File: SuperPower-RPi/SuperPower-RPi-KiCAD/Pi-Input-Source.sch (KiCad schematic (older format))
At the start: 0 parts

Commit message: Added Input Protection Circuit for MWB.
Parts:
- added J?: Screw_Terminal_01x02, symbol Connector:Screw_Terminal_01x02
- added P1: USB_C_Plug, symbol Connector:USB_C_Plug
- added Q3: Q_PMOS_GSD, symbol Device:Q_PMOS_GSD
- added R3: 1k?, symbol Device:R
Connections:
- net labels added: GND
- wire segments 0 -> 14
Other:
- note added: "Primary USB Power Input"
- note added: "Solar or Other Input Power"
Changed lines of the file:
@@
 Comment4 ""
 $EndDescr
-Text HLabel 7600 2900 0    50   Output ~ 0
+Text HLabel 7300 2900 2    50   Output ~ 0
 Vout
-Text Notes 2350 4000 0    50   ~ 0
+Text Notes 6950 5750 0    50   ~ 0
 NOTE:\nProbably USB-C and screw-terminals for solar.  MicroUSB possible.
+$Comp
+L Device:Q_PMOS_GSD Q3
+U 1 1 5F703042
+P 6950 3000
+F 0 "Q3" V 7292 3000 50  0000 C CNN
+F 1 "Q_PMOS_GSD" V 7201 3000 50  0000 C CNN
+F 2 "" H 7150 3100 50  0001 C CNN
+F 3 "~" H 6950 3000 50  0001 C CNN
+	1    6950 3000
+	0    -1   -1   0
+$EndComp
+$Comp
+L power:GND #PWR05
+U 1 1 5F703EB6
+P 6950 3850
+F 0 "#PWR05" H 6950 3600 50  0001 C CNN
+F 1 "GND" H 6955 3677 50  0000 C CNN
+F 2 "" H 6950 3850 50  0001 C CNN
+F 3 "" H 6950 3850 50  0001 C CNN
+	1    6950 3850
+	1    0    0    -1
+$EndComp
+$Comp
+L Connector:USB_C_Plug P1
+U 1 1 5F704D8C
+P 4550 3900
+F 0 "P1" H 4657 5167 50  0000 C CNN
+F 1 "USB_C_Plug" H 4657 5076 50  0000 C CNN
+F 2 "" H 4700 3900 50  0001 C CNN
+F 3 "https://www.usb.org/sites/default/files/documents/usb_type-c.zip" H 4700 3900 50  0001 C CNN
+	1    4550 3900
+	1    0    0    -1
+$EndComp
+$Comp
+L power:GND #PWR04
+U 1 1 5F709AD2
+P 4400 5750
+F 0 "#PWR04" H 4400 5500 50  0001 C CNN
+F 1 "GND" H 4405 5577 50  0000 C CNN
+F 2 "" H 4400 5750 50  0001 C CNN
+F 3 "" H 4400 5750 50  0001 C CNN
+	1    4400 5750
+	1    0    0    -1
+$EndComp
+Wire Wire Line
+	4250 5500 4250 5650
+Wire Wire Line
+	4250 5650 4400 5650
+Wire Wire Line
+	4550 5650 4550 5500
+Wire Wire Line
+	4400 5750 4400 5650
+Connection ~ 4400 5650
+Wire Wire Line
+	4400 5650 4550 5650
+$Comp
+L Device:R R3
+U 1 1 5F70A531
+P 6950 3500
+F 0 "R3" H 7020 3546 50  0000 L CNN
+F 1 "1k?" H 7020 3455 50  0000 L CNN
+F 2 "" V 6880 3500 50  0001 C CNN
+F 3 "~" H 6950 3500 50  0001 C CNN
+	1    6950 3500
+	1    0    0    -1
+$EndComp
+Wire Wire Line
+	6950 3350 6950 3200
+Wire Wire Line
+	6950 3650 6950 3850
+Wire Wire Line
+	7150 2900 7300 2900
+Wire Wire Line
+	5150 2900 5550 2900
+Text Notes 4150 6150 0    50   ~ 0
+Primary USB Power Input
+$Comp
+L Connector:Screw_Terminal_01x02 J?
+U 1 1 5F70C370
+P 4500 1750
+F 0 "J?" H 4418 1425 50  0000 C CNN
+F 1 "Screw_Terminal_01x02" H 4418 1516 50  0000 C CNN
+F 2 "" H 4500 1750 50  0001 C CNN
+F 3 "~" H 4500 1750 50  0001 C CNN
+	1    4500 1750
+	-1   0    0    1
+$EndComp
+Wire Wire Line
+	4700 1650 5550 1650
+Wire Wire Line
+	5550 1650 5550 2900
+Connection ~ 5550 2900
+Wire Wire Line
+	5550 2900 6750 2900
+$Comp
+L power:GND #PWR?
+U 1 1 5F70CF53
+P 4750 1800
+F 0 "#PWR?" H 4750 1550 50  0001 C CNN
+F 1 "GND" H 4755 1627 50  0000 C CNN
+F 2 "" H 4750 1800 50  0001 C CNN
+F 3 "" H 4750 1800 50  0001 C CNN
+	1    4750 1800
+	1    0    0    -1
+$EndComp
+Wire Wire Line
+	4700 1750 4750 1750
+Wire Wire Line
+	4750 1750 4750 1800
+Text Notes 4100 2100 0    50   ~ 0
+Solar or Other Input Power
 $EndSCHEMATC

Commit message: Added charger circuitry, and updated boost converter.
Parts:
- gave numbers to parts that had none: 1
- renumbered R3 to R12
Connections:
- net labels added: D+, D-
- wire segments 14 -> 18
- no-connect marks 0 -> 12
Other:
- note added: "Should the USB VBUS be moved to after the input protection?"
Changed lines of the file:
@@
 $EndComp
 $Comp
-L power:GND #PWR05
+L power:GND #PWR0101
 U 1 1 5F703EB6
 P 6950 3850
-F 0 "#PWR05" H 6950 3600 50  0001 C CNN
+F 0 "#PWR0101" H 6950 3600 50  0001 C CNN
 F 1 "GND" H 6955 3677 50  0000 C CNN
 F 2 "" H 6950 3850 50  0001 C CNN
@@
 $EndComp
 $Comp
-L power:GND #PWR04
+L power:GND #PWR0102
 U 1 1 5F709AD2
 P 4400 5750
-F 0 "#PWR04" H 4400 5500 50  0001 C CNN
+F 0 "#PWR0102" H 4400 5500 50  0001 C CNN
 F 1 "GND" H 4405 5577 50  0000 C CNN
 F 2 "" H 4400 5750 50  0001 C CNN
@@
 	4400 5650 4550 5650
 $Comp
-L Device:R R3
+L Device:R R12
 U 1 1 5F70A531
 P 6950 3500
-F 0 "R3" H 7020 3546 50  0000 L CNN
+F 0 "R12" H 7020 3546 50  0000 L CNN
 F 1 "1k?" H 7020 3455 50  0000 L CNN
 F 2 "" V 6880 3500 50  0001 C CNN
@@
 Primary USB Power Input
 $Comp
-L Connector:Screw_Terminal_01x02 J?
+L Connector:Screw_Terminal_01x02 J3
 U 1 1 5F70C370
 P 4500 1750
-F 0 "J?" H 4418 1425 50  0000 C CNN
+F 0 "J3" H 4418 1425 50  0000 C CNN
 F 1 "Screw_Terminal_01x02" H 4418 1516 50  0000 C CNN
 F 2 "" H 4500 1750 50  0001 C CNN
@@
 Connection ~ 5550 2900
 Wire Wire Line
-	5550 2900 6750 2900
+	5550 2900 5800 2900
 $Comp
-L power:GND #PWR?
+L power:GND #PWR010
 U 1 1 5F70CF53
 P 4750 1800
-F 0 "#PWR?" H 4750 1550 50  0001 C CNN
+F 0 "#PWR010" H 4750 1550 50  0001 C CNN
 F 1 "GND" H 4755 1627 50  0000 C CNN
 F 2 "" H 4750 1800 50  0001 C CNN
@@
 Text Notes 4100 2100 0    50   ~ 0
 Solar or Other Input Power
+$Comp
+L power:PWR_FLAG #FLG0101
+U 1 1 5F7A3576
+P 4800 1750
+F 0 "#FLG0101" H 4800 1825 50  0001 C CNN
+F 1 "PWR_FLAG" V 4800 1878 50  0001 L CNN
+F 2 "" H 4800 1750 50  0001 C CNN
+F 3 "~" H 4800 1750 50  0001 C CNN
+	1    4800 1750
+	0    1    1    0
+$EndComp
+Wire Wire Line
+	4800 1750 4750 1750
+Connection ~ 4750 1750
+$Comp
+L power:PWR_FLAG #FLG0102
+U 1 1 5F7A5141
+P 5800 2900
+F 0 "#FLG0102" H 5800 2975 50  0001 C CNN
+F 1 "PWR_FLAG" V 5800 3028 50  0001 L CNN
+F 2 "" H 5800 2900 50  0001 C CNN
+F 3 "~" H 5800 2900 50  0001 C CNN
+	1    5800 2900
+	1    0    0    -1
+$EndComp
+Connection ~ 5800 2900
+Wire Wire Line
+	5800 2900 6750 2900
+NoConn ~ 5150 5200
+NoConn ~ 5150 5100
+NoConn ~ 5150 4900
+NoConn ~ 5150 4800
+NoConn ~ 5150 4600
+NoConn ~ 5150 4500
+NoConn ~ 5150 4300
+NoConn ~ 5150 4200
+NoConn ~ 5150 4000
+NoConn ~ 5150 3900
+NoConn ~ 5150 3200
+NoConn ~ 5150 3100
+Text HLabel 5400 3600 2    50   Output ~ 0
+D+
+Text HLabel 5400 3400 2    50   Output ~ 0
+D-
+Wire Wire Line
+	5400 3400 5150 3400
+Wire Wire Line
+	5150 3600 5400 3600
+Text Notes 6250 2050 0    50   ~ 0
+Should the USB VBUS be moved to after the input protection?
 $EndSCHEMATC

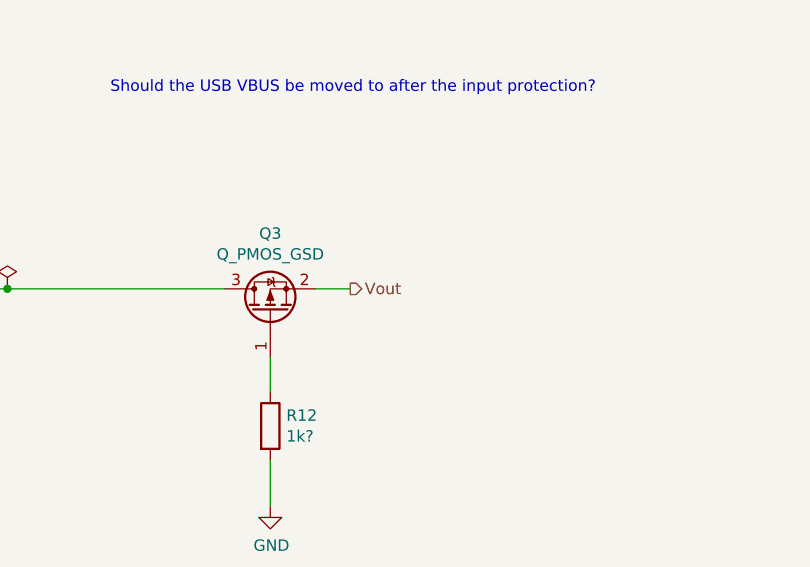
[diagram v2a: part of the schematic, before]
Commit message: Updated TPS61088 part to clear up ERC errors.
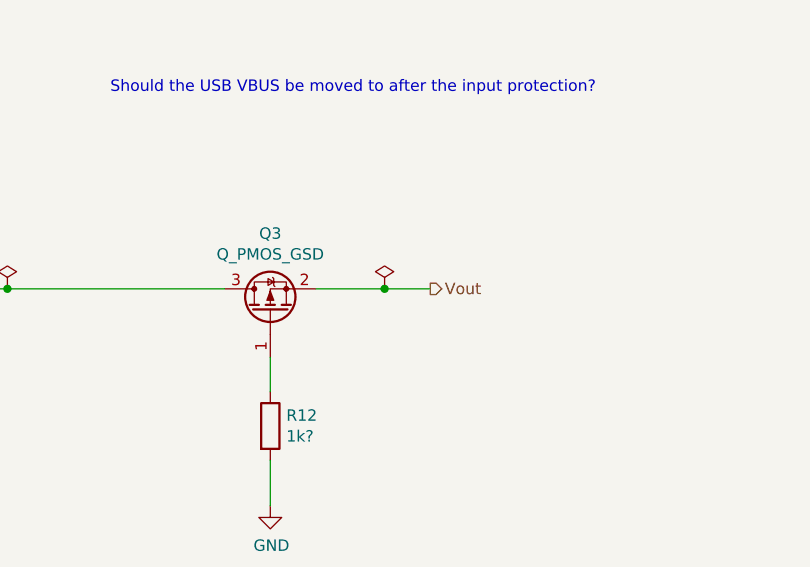
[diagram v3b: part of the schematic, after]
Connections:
- wire segments 18 -> 19
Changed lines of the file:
@@
 Comment4 ""
 $EndDescr
-Text HLabel 7300 2900 2    50   Output ~ 0
+Text HLabel 7650 2900 2    50   Output ~ 0
 Vout
 Text Notes 6950 5750 0    50   ~ 0
@@
 	6950 3650 6950 3850
 Wire Wire Line
-	7150 2900 7300 2900
+	7150 2900 7450 2900
 Wire Wire Line
 	5150 2900 5550 2900
@@
 Text Notes 6250 2050 0    50   ~ 0
 Should the USB VBUS be moved to after the input protection?
+$Comp
+L power:PWR_FLAG #FLG0106
+U 1 1 5F79AC3D
+P 7450 2900
+F 0 "#FLG0106" H 7450 2975 50  0001 C CNN
+F 1 "PWR_FLAG" V 7450 3028 50  0001 L CNN
+F 2 "" H 7450 2900 50  0001 C CNN
+F 3 "~" H 7450 2900 50  0001 C CNN
+	1    7450 2900
+	1    0    0    -1
+$EndComp
+Connection ~ 7450 2900
+Wire Wire Line
+	7450 2900 7650 2900
 $EndSCHEMATC

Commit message: Changed connector from USB-C to USB-C USB2.0
(cherry picked from commit 57ca05fac51607dd5300f81bf9f2e7d7ab65204a)
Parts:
- removed P1: USB_C_Plug, symbol Connector:USB_C_Plug
- added P?: USB_C_Plug_USB2.0, symbol Connector:USB_C_Plug_USB2.0
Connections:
- no-connect marks 12 -> 2
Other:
- note added: "NOTE:\nProbably USB-C and screw-terminals for solar. \nMicroUSB possible."
- note removed: "NOTE:\nProbably USB-C and screw-terminals for solar. MicroUSB possible."
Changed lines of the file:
@@
 Vout
 Text Notes 6950 5750 0    50   ~ 0
-NOTE:\nProbably USB-C and screw-terminals for solar.  MicroUSB possible.
+NOTE:\nProbably USB-C and screw-terminals for solar.  \nMicroUSB possible.
 $Comp
 L Device:Q_PMOS_GSD Q3
@@
 $EndComp
 $Comp
-L Connector:USB_C_Plug P1
-U 1 1 5F704D8C
-P 4550 3900
-F 0 "P1" H 4657 5167 50  0000 C CNN
-F 1 "USB_C_Plug" H 4657 5076 50  0000 C CNN
-F 2 "" H 4700 3900 50  0001 C CNN
-F 3 "https://www.usb.org/sites/default/files/documents/usb_type-c.zip" H 4700 3900 50  0001 C CNN
-	1    4550 3900
-	1    0    0    -1
-$EndComp
-$Comp
 L power:GND #PWR0102
 U 1 1 5F709AD2
-P 4400 5750
-F 0 "#PWR0102" H 4400 5500 50  0001 C CNN
-F 1 "GND" H 4405 5577 50  0000 C CNN
-F 2 "" H 4400 5750 50  0001 C CNN
-F 3 "" H 4400 5750 50  0001 C CNN
-	1    4400 5750
+P 4400 4650
+F 0 "#PWR0102" H 4400 4400 50  0001 C CNN
+F 1 "GND" H 4405 4477 50  0000 C CNN
+F 2 "" H 4400 4650 50  0001 C CNN
+F 3 "" H 4400 4650 50  0001 C CNN
+	1    4400 4650
 	1    0    0    -1
 $EndComp
 Wire Wire Line
-	4250 5500 4250 5650
+	4250 4400 4250 4550
 Wire Wire Line
-	4250 5650 4400 5650
+	4250 4550 4400 4550
 Wire Wire Line
-	4550 5650 4550 5500
+	4550 4550 4550 4400
 Wire Wire Line
-	4400 5750 4400 5650
-Connection ~ 4400 5650
+	4400 4650 4400 4550
+Connection ~ 4400 4550
 Wire Wire Line
-	4400 5650 4550 5650
+	4400 4550 4550 4550
 $Comp
 L Device:R R12
@@
 Wire Wire Line
 	5150 2900 5550 2900
-Text Notes 4150 6150 0    50   ~ 0
+Text Notes 4150 5050 0    50   ~ 0
 Primary USB Power Input
 $Comp
@@
 Wire Wire Line
 	5800 2900 6750 2900
-NoConn ~ 5150 5200
-NoConn ~ 5150 5100
-NoConn ~ 5150 4900
-NoConn ~ 5150 4800
-NoConn ~ 5150 4600
-NoConn ~ 5150 4500
-NoConn ~ 5150 4300
-NoConn ~ 5150 4200
-NoConn ~ 5150 4000
-NoConn ~ 5150 3900
-NoConn ~ 5150 3200
-NoConn ~ 5150 3100
 Text HLabel 5400 3600 2    50   Output ~ 0
 D+
@@
 Wire Wire Line
 	7450 2900 7650 2900
+$Comp
+L Connector:USB_C_Plug_USB2.0 P?
+U 1 1 5FA09B52
+P 4550 3500
+F 0 "P?" H 4657 4367 50  0000 C CNN
+F 1 "USB_C_Plug_USB2.0" H 4657 4276 50  0000 C CNN
+F 2 "" H 4700 3500 50  0001 C CNN
+F 3 "https://www.usb.org/sites/default/files/documents/usb_type-c.zip" H 4700 3500 50  0001 C CNN
+	1    4550 3500
+	1    0    0    -1
+$EndComp
+NoConn ~ 5150 3200
+NoConn ~ 5150 3100
 $EndSCHEMATC

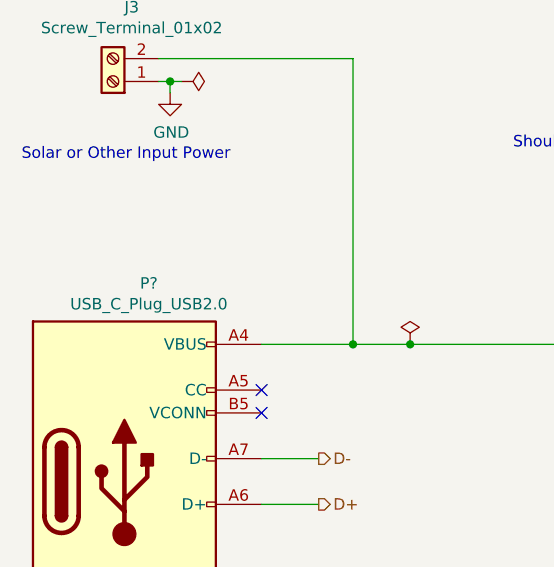
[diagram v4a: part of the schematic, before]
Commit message: Annotated schematic and wiring up MCUs.
(cherry picked from commit e13d5e6812bbd71083f4554307639845a5fce7af)
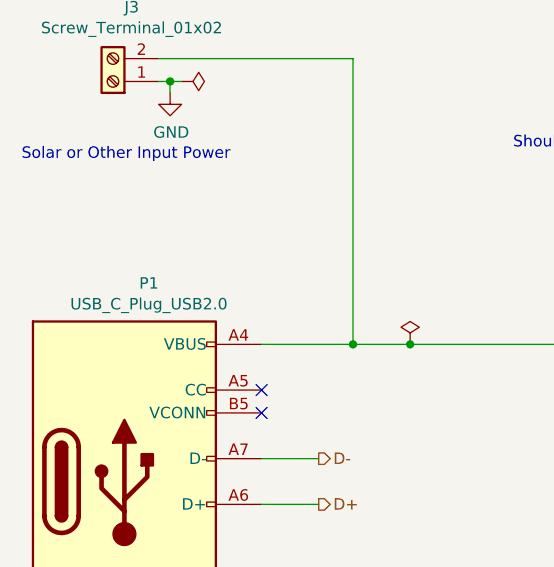
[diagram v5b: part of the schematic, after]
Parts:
- gave numbers to parts that had none: 1
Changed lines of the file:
@@
 	7450 2900 7650 2900
 $Comp
-L Connector:USB_C_Plug_USB2.0 P?
+L Connector:USB_C_Plug_USB2.0 P1
 U 1 1 5FA09B52
 P 4550 3500
-F 0 "P?" H 4657 4367 50  0000 C CNN
+F 0 "P1" H 4657 4367 50  0000 C CNN
 F 1 "USB_C_Plug_USB2.0" H 4657 4276 50  0000 C CNN
 F 2 "" H 4700 3500 50  0001 C CNN

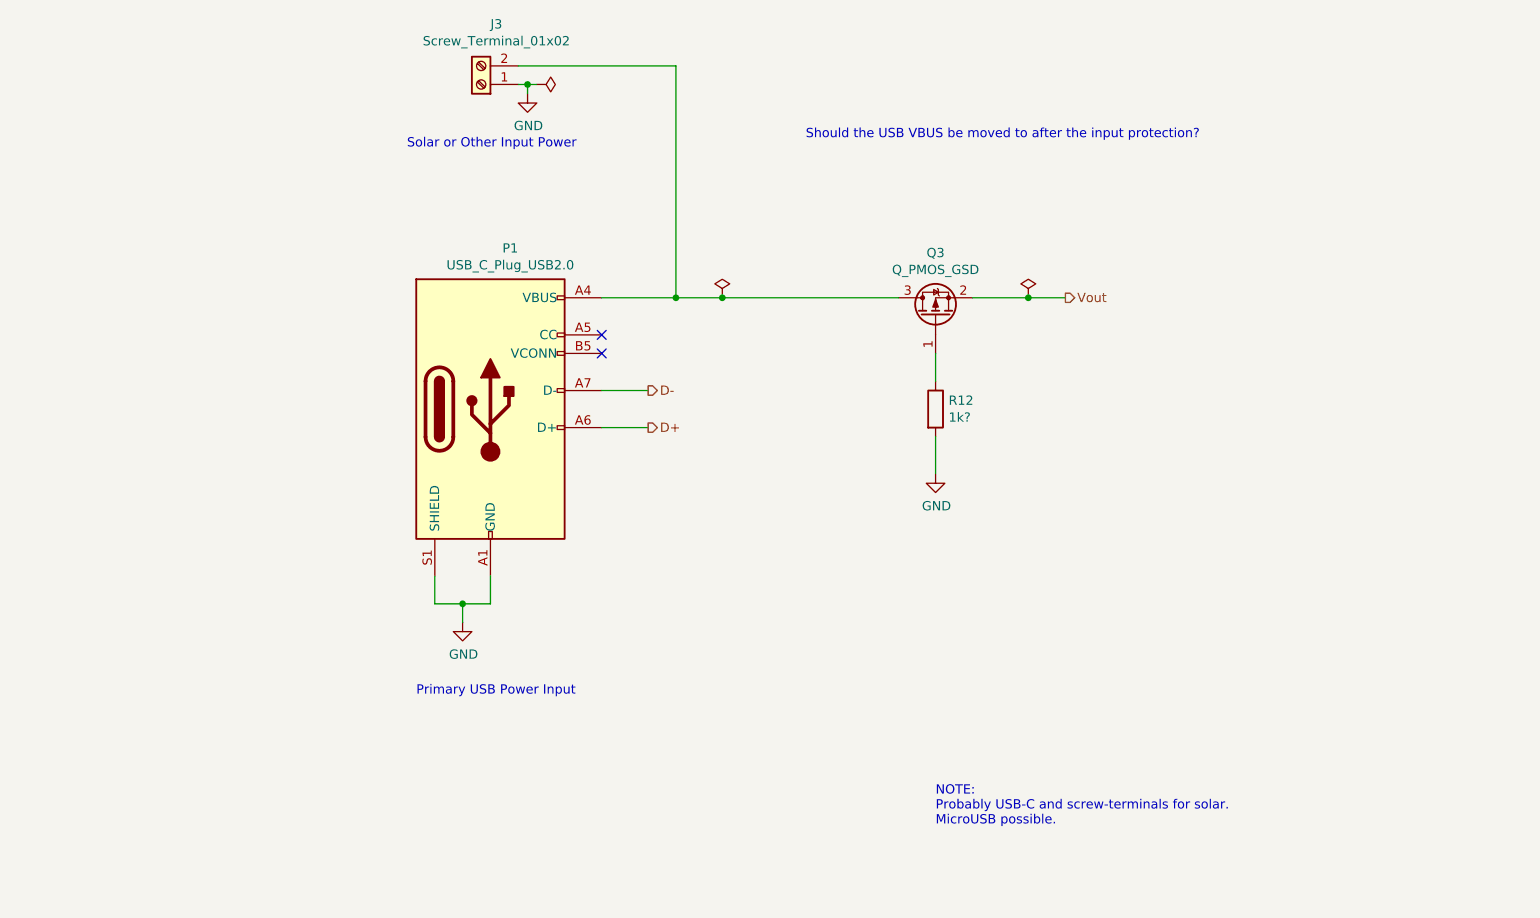
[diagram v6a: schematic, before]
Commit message: Added overvoltag protection. Discussed on discord on 10/10/2020
(cherry picked from commit 123c8c775d478169a35a5854a68dc219ac457a44)
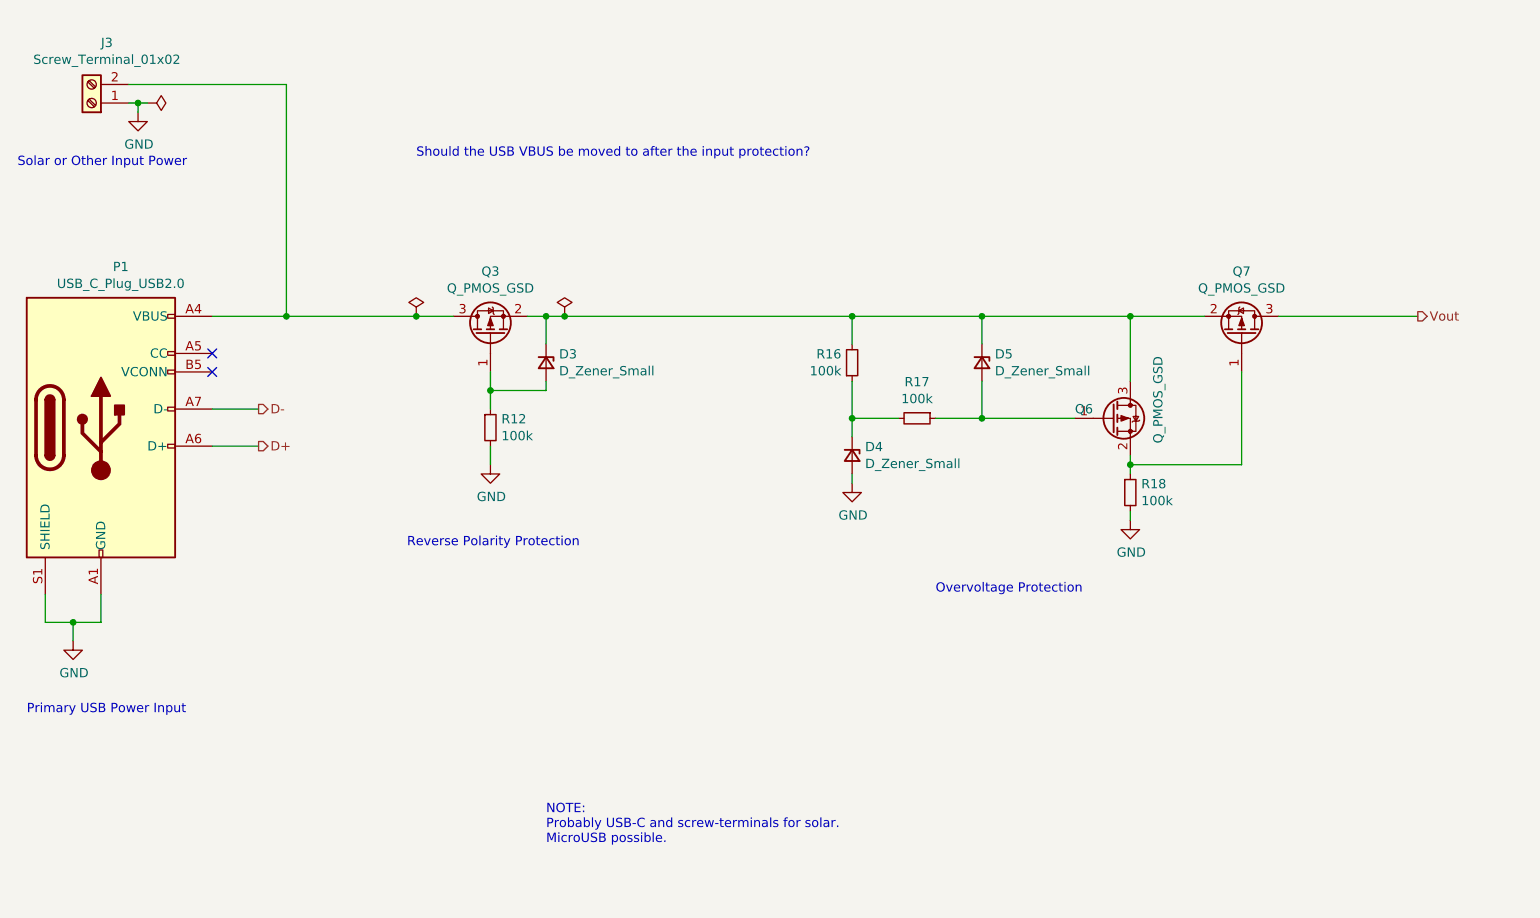
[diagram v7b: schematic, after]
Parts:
- removed R12: 1k?, symbol Device:R
- added D3, D4, D5: D_Zener_Small, symbol Device:D_Zener_Small
- added Q6, Q7: Q_PMOS_GSD, symbol Device:Q_PMOS_GSD
- added R12, R16, R17, R18: 100k, Resistor_SMD:R_0603_1608Metric, symbol Device:R_Small
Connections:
- net GND: now also D4.2 (A), R12.2, R18.2
- net Vout: now also Q7.3 (D); no longer Q3.2 (S)
- net at Q3.1 (G): now also D3.2 (A), R12.1
- new net: D3.1 (K), D5.1 (K), Q3.2 (S), Q6.3 (D), Q7.2 (S), R16.2
- new net: D4.1 (K), R16.1, R17.2
- new net: D5.2 (A), Q6.1 (G), R17.1
- new net: Q6.2 (S), Q7.1 (G), R18.1
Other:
- note added: "Overvoltage Protection"
- note added: "Reverse Polarity Protection"
- moved on the sheet: J3, P1, Q3

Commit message: Updated components. Mostly caps and resistors.
(cherry picked from commit e921c80666429be92cc496d87bcbd557350196b5)
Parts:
- R12, R16, R17, R18: Digi-Key PN (none) -> 311-100KHRCT-ND; Mfg (none) -> Yageo; Mfg PN (none) -> RC0603FR-07100KL
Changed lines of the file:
@@
 F 2 "Resistor_SMD:R_0603_1608Metric" H 4550 3600 50  0001 C CNN
 F 3 "~" H 4550 3600 50  0001 C CNN
+F 4 "311-100KHRCT-ND" H 4550 3600 50  0001 C CNN "Digi-Key PN"
+F 5 "Yageo" H 4550 3600 50  0001 C CNN "Mfg"
+F 6 "RC0603FR-07100KL" H 4550 3600 50  0001 C CNN "Mfg PN"
 	1    4550 3600
 	1    0    0    -1
@@
 F 2 "Resistor_SMD:R_0603_1608Metric" H 6500 3250 50  0001 C CNN
 F 3 "~" H 6500 3250 50  0001 C CNN
+F 4 "311-100KHRCT-ND" H 6500 3250 50  0001 C CNN "Digi-Key PN"
+F 5 "Yageo" H 6500 3250 50  0001 C CNN "Mfg"
+F 6 "RC0603FR-07100KL" H 6500 3250 50  0001 C CNN "Mfg PN"
 	1    6500 3250
 	1    0    0    1
@@
 F 2 "Resistor_SMD:R_0603_1608Metric" H 6850 3550 50  0001 C CNN
 F 3 "~" H 6850 3550 50  0001 C CNN
+F 4 "311-100KHRCT-ND" H 6850 3550 50  0001 C CNN "Digi-Key PN"
+F 5 "Yageo" H 6850 3550 50  0001 C CNN "Mfg"
+F 6 "RC0603FR-07100KL" H 6850 3550 50  0001 C CNN "Mfg PN"
 	1    6850 3550
 	0    1    1    0
@@
 F 2 "Resistor_SMD:R_0603_1608Metric" H 8000 3950 50  0001 C CNN
 F 3 "~" H 8000 3950 50  0001 C CNN
+F 4 "311-100KHRCT-ND" H 8000 3950 50  0001 C CNN "Digi-Key PN"
+F 5 "Yageo" H 8000 3950 50  0001 C CNN "Mfg"
+F 6 "RC0603FR-07100KL" H 8000 3950 50  0001 C CNN "Mfg PN"
 	1    8000 3950
 	1    0    0    -1
